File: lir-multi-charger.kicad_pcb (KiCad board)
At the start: 2 copper layers, 90 x 58 mm, 57 parts, among them J1 USB_C_Receptacle_USB2.0, J11 Conn_01x01_Male, J12 Conn_01x01_Male, J2 Conn_01x02_Male, J3 Conn_01x02_Male, J4 Conn_01x02_Male, J5 Conn_01x02_Male, J6 Conn_01x02_Male, U1 TP4056, U2 TP4056, U3 TP4056

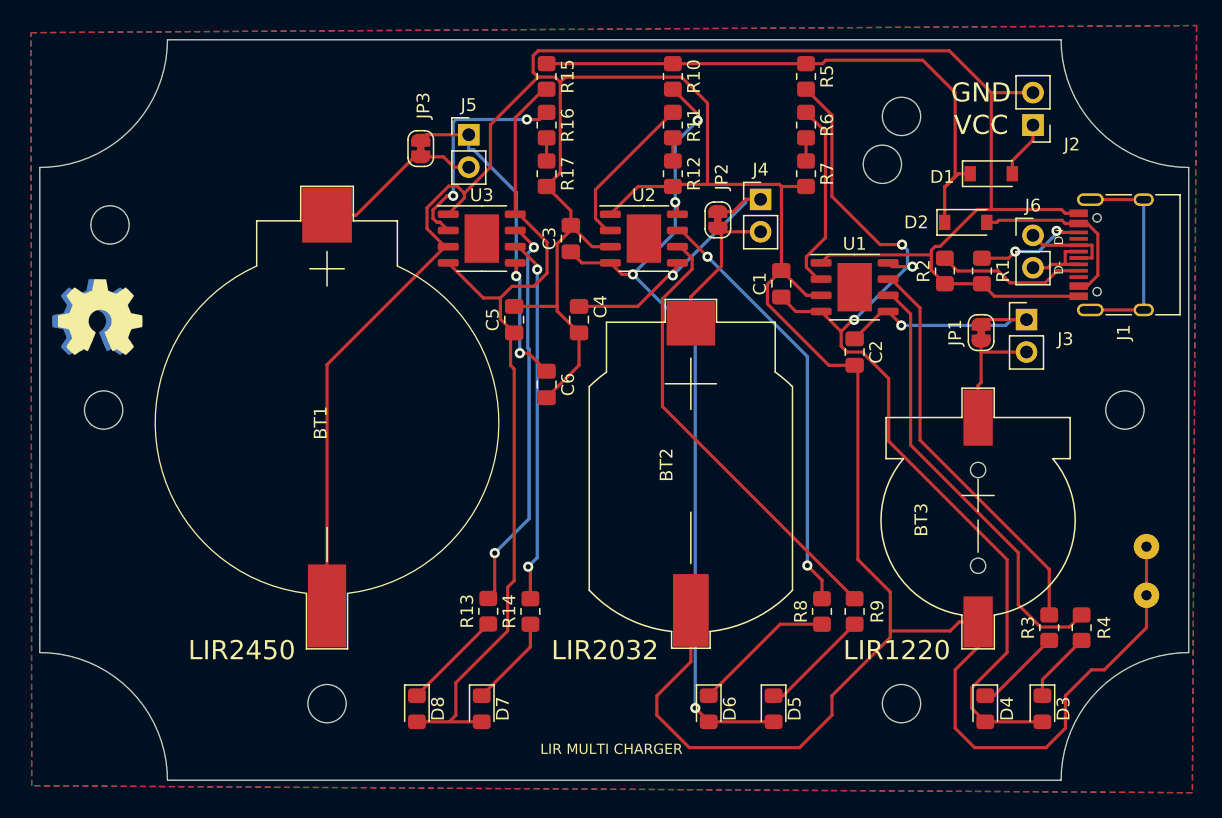
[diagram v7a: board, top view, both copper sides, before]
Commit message: changed charger IC
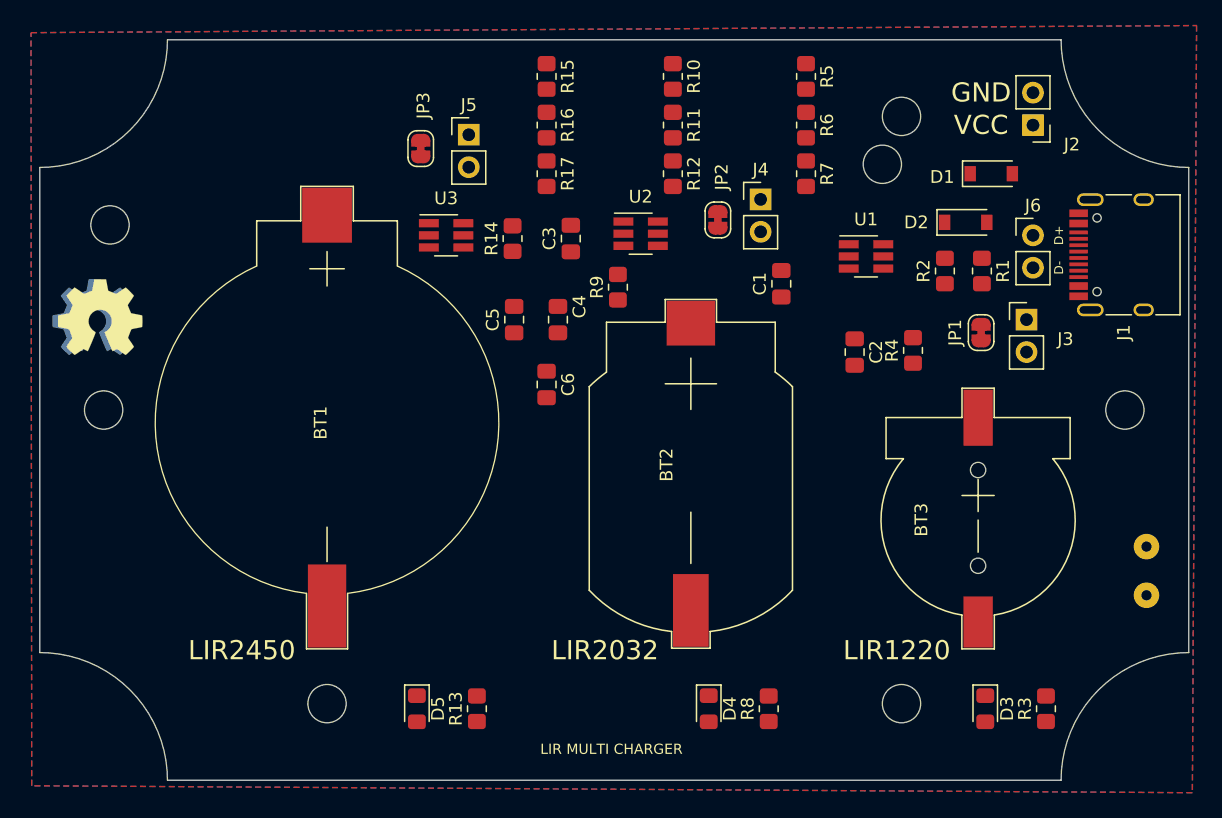
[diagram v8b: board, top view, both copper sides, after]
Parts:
- removed the D3 at (178.5, 152.4)
- removed the D5 at (157.5, 152.4)
- removed D7: GREEN, LED_SMD:LED_0805_2012Metric_Pad1.15x1.40mm_HandSolder
- R14, R4, R9: value 1k -> 0R
- U1, U2, U3: value TP4056 -> CN3130; footprint Li-ion-charger:tp4056 -> Package_TO_SOT_SMD:SOT-23-6_Handsoldering
- moved R9 31.4 mm to (145.3, 119.4)
- moved R14 29.2 mm to (137.0, 115.6)
- moved R4 25.4 mm to (168.4, 124.3)
- moved R8 8.69 mm to (157.1, 152.4)
- moved R13 7.69 mm to (134.2, 152.4)
- moved R3 6.36 mm to (178.8, 152.4)
- moved U3 2.81 mm to (131.8, 115.3)
- moved U1 2.57 mm to (164.7, 117.0)
- moved C4 1.65 mm to (140.6, 121.9)
- moved U2 0.46 mm to (147.1, 115.2)
- renumbered D4 to D3, D6 to D4, D8 to D5
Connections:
- C1 pad 1: Net-(C1-Pad1) -> Net-(R5-Pad2)
- C5 pad 1: Net-(C5-Pad1) -> Net-(R15-Pad2)
- D3 pad 2: Net-(C1-Pad1) -> Net-(R5-Pad2)
- D5 pad 2: Net-(C5-Pad1) -> Net-(R15-Pad2)
- R14 pad 1: Net-(D7-Pad1) -> Net-(C6-Pad1)
- R15 pad 2: Net-(C5-Pad1) -> Net-(R15-Pad2)
- R4 pad 1: Net-(D3-Pad1) (its old number) -> Net-(C2-Pad1)
- R4 pad 2: Net-(R4-Pad2) -> Net-(U1-Pad2)
- R5 pad 2: Net-(C1-Pad1) -> Net-(R5-Pad2)
- R9 pad 1: Net-(D5-Pad1) (its old number) -> Net-(C4-Pad1)
- U1 pad 1: GND -> Net-(R3-Pad2)
- U1 pad 2: Net-(R6-Pad1) -> Net-(U1-Pad2)
- U1 pad 3: GND -> Net-(C2-Pad1)
- U1 pad 4: Net-(C1-Pad1) -> Net-(R5-Pad2)
- U1 pad 5: Net-(C2-Pad1) -> GND
- U1 pad 6: Net-(R4-Pad2) -> Net-(R6-Pad1)
- U2 pad 1: GND -> Net-(R8-Pad2)
- U2 pad 2: Net-(R11-Pad1) -> Net-(R9-Pad2)
- U2 pad 3: GND -> Net-(C4-Pad1)
- U2 pad 5: Net-(C4-Pad1) -> GND
- U2 pad 6: Net-(R9-Pad2) -> Net-(R11-Pad1)
- U3 pad 1: GND -> Net-(R13-Pad2)
- U3 pad 2: Net-(R16-Pad1) -> Net-(R14-Pad2)
- U3 pad 3: GND -> Net-(C6-Pad1)
- U3 pad 4: Net-(C5-Pad1) -> Net-(R15-Pad2)
- U3 pad 5: Net-(C6-Pad1) -> GND
- U3 pad 6: Net-(R14-Pad2) -> Net-(R16-Pad1)
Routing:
- net GND: track 334.8 -> 0.00 mm
- net Net-(C1-Pad1): track 76.4 -> 0.00 mm, vias 3 -> 0
- net Net-(C5-Pad1): track 67.5 -> 0.00 mm
- net Net-(C3-Pad1): track 66.6 -> 0.00 mm, vias 4 -> 0
- net VBUS: track 46.1 -> 0.00 mm
- net Net-(R9-Pad2): track 35.4 -> 0.00 mm
- net Net-(R4-Pad2): track 34.7 -> 0.00 mm
- net Net-(R8-Pad2): track 33.7 -> 0.00 mm, vias 2 -> 0
- net Net-(R3-Pad2): track 31.7 -> 0.00 mm
- net Net-(R13-Pad2): track 31.1 -> 0.00 mm, vias 2 -> 0
- net Net-(R14-Pad2): track 28.8 -> 0.00 mm, vias 2 -> 0
- net Net-(C6-Pad1): track 26.7 -> 0.00 mm, vias 2 -> 0
- net Net-(C4-Pad1): track 22.8 -> 0.00 mm, vias 1 -> 0
- net Net-(C2-Pad1): track 18.7 -> 0.00 mm, vias 1 -> 0
- net Net-(R16-Pad1): track 17.7 -> 0.00 mm, vias 2 -> 0
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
